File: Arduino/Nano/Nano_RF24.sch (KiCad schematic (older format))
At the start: 3 parts, among them P1 NRF24L01+, U1 Arduino_Nano

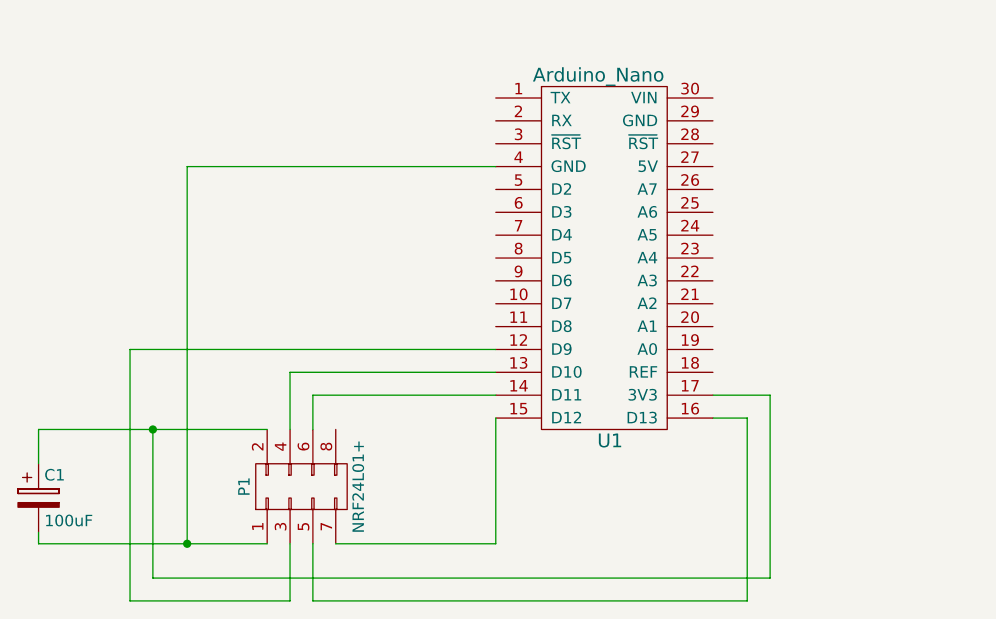
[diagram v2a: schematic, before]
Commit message: v2 with breakout pins
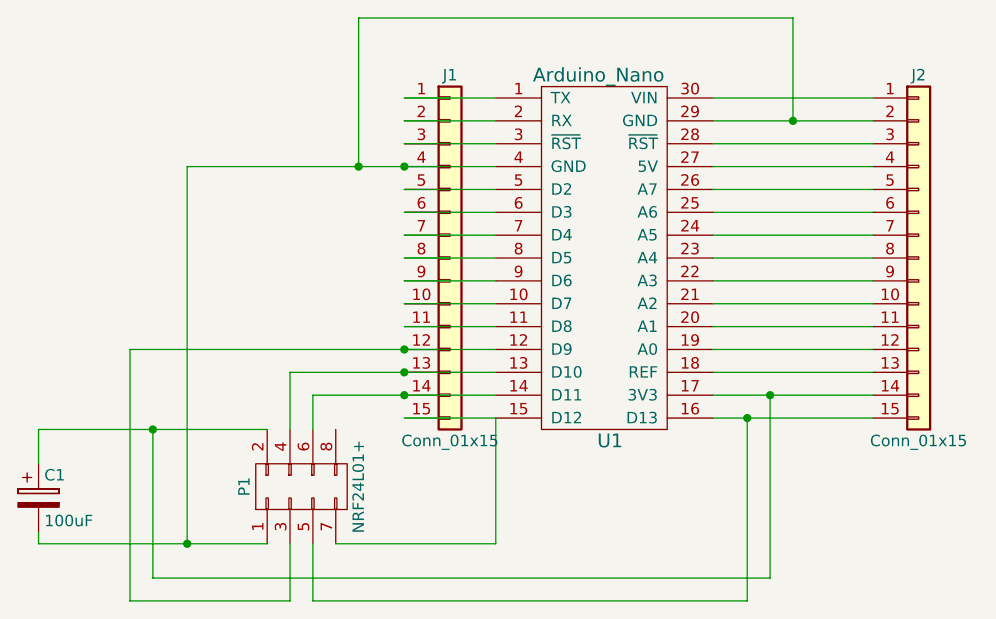
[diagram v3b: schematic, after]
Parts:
- added J1, J2: Conn_01x15, Pin_Headers:Pin_Header_Straight_1x15_Pitch2.54mm, symbol Conn_01x15
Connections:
- net at U1.1 (TX): now also J1.1 (Pin_1)
- net at U1.10 (D7): now also J1.10 (Pin_10)
- net at U1.11 (D8): now also J1.11 (Pin_11)
- net at P1.3 (P3), U1.12 (D9): now also J1.12 (Pin_12)
- net at P1.4 (P4), U1.13 (D10): now also J1.13 (Pin_13)
- net at P1.6 (P6), U1.14 (D11): now also J1.14 (Pin_14)
- net at P1.7 (P7), U1.15 (D12): now also J1.15 (Pin_15)
- net at P1.5 (P5), U1.16 (D13): now also J2.15 (Pin_15)
- net at C1.1, P1.2 (P2), U1.17 (3V3): now also J2.14 (Pin_14)
- net at U1.18 (REF): now also J2.13 (Pin_13)
- net at U1.19 (A0): now also J2.12 (Pin_12)
- net at U1.2 (RX): now also J1.2 (Pin_2)
- net at U1.20 (A1): now also J2.11 (Pin_11)
- net at U1.21 (A2): now also J2.10 (Pin_10)
- net at U1.22 (A3): now also J2.9 (Pin_9)
- net at U1.23 (A4): now also J2.8 (Pin_8)
- net at U1.24 (A5): now also J2.7 (Pin_7)
- net at U1.25 (A6): now also J2.6 (Pin_6)
- net at U1.26 (A7): now also J2.5 (Pin_5)
- net at U1.27 (5V): now also J2.4 (Pin_4)
- net at U1.28 (~RST): now also J2.3 (Pin_3)
- net at U1.29 (GND): now also C1.2, P1.1 (P1), U1.4 (GND), J1.4 (Pin_4), J2.2 (Pin_2)
- net at U1.3 (~RST): now also J1.3 (Pin_3)
- net at U1.30 (VIN): now also J2.1 (Pin_1)
- net at U1.5 (D2): now also J1.5 (Pin_5)
- net at U1.6 (D3): now also J1.6 (Pin_6)
- net at U1.7 (D4): now also J1.7 (Pin_7)
- net at U1.8 (D5): now also J1.8 (Pin_8)
- net at U1.9 (D6): now also J1.9 (Pin_9)
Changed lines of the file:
@@
 Title "Arduino Nano NRF24L01+ Adaptor"
 Date "2018-03-30"
-Rev "1"
+Rev "2"
 Comp ""
 Comment1 "Copyright Mark Benson 2018"
@@
 $EndComp
 Wire Wire Line
-	4900 3150 3550 3150
-Wire Wire Line
 	3550 3150 3550 4800
 Wire Wire Line
@@
 	6100 4950 6100 4150
 Wire Wire Line
-	6100 4150 5850 4150
+	5850 4150 6550 4150
 Wire Wire Line
 	4000 4800 4000 5050
@@
 	3300 5050 3300 3950
 Wire Wire Line
-	3300 3950 4900 3950
-Wire Wire Line
 	4000 4300 4000 4050
-Wire Wire Line
-	4000 4050 4900 4050
 Wire Wire Line
 	4100 4800 4100 5050
@@
 	6000 5050 6000 4250
 Wire Wire Line
-	6000 4250 5850 4250
+	5850 4250 6550 4250
 Wire Wire Line
 	4100 4300 4100 4150
-Wire Wire Line
-	4100 4150 4900 4150
 Wire Wire Line
 	4200 4800 4900 4800
@@
 	2900 4300 2900 4450
 Connection ~ 3400 4300
+$Comp
+L Conn_01x15 J2
+U 1 1 5ABE09D5
+P 6750 3550
+F 0 "J2" H 6750 4350 50  0000 C CNN
+F 1 "Conn_01x15" H 6750 2750 50  0000 C CNN
+F 2 "Pin_Headers:Pin_Header_Straight_1x15_Pitch2.54mm" H 6750 3550 50  0001 C CNN
+F 3 "" H 6750 3550 50  0001 C CNN
+	1    6750 3550
+	1    0    0    -1
+$EndComp
+$Comp
+L Conn_01x15 J1
+U 1 1 5ABE09F4
+P 4700 3550
+F 0 "J1" H 4700 4350 50  0000 C CNN
+F 1 "Conn_01x15" H 4700 2750 50  0000 C CNN
+F 2 "Pin_Headers:Pin_Header_Straight_1x15_Pitch2.54mm" H 4700 3550 50  0001 C CNN
+F 3 "" H 4700 3550 50  0001 C CNN
+	1    4700 3550
+	1    0    0    -1
+$EndComp
+Wire Wire Line
+	5850 2850 6550 2850
+Wire Wire Line
+	5850 2950 6550 2950
+Wire Wire Line
+	5850 3050 6550 3050
+Wire Wire Line
+	5850 3150 6550 3150
+Wire Wire Line
+	5850 3250 6550 3250
+Wire Wire Line
+	5850 3350 6550 3350
+Wire Wire Line
+	5850 3450 6550 3450
+Wire Wire Line
+	5850 3550 6550 3550
+Wire Wire Line
+	6550 3650 5850 3650
+Wire Wire Line
+	5850 3750 6550 3750
+Wire Wire Line
+	5850 3850 6550 3850
+Wire Wire Line
+	5850 3950 6550 3950
+Wire Wire Line
+	5850 4050 6550 4050
+Connection ~ 6100 4150
+Connection ~ 6000 4250
+Wire Wire Line
+	4500 2850 4900 2850
+Wire Wire Line
+	4900 2950 4500 2950
+Wire Wire Line
+	4500 3050 4900 3050
+Wire Wire Line
+	4500 3250 4900 3250
+Wire Wire Line
+	4500 3350 4900 3350
+Wire Wire Line
+	3550 3150 4900 3150
+Connection ~ 4500 3150
+Wire Wire Line
+	4900 3450 4500 3450
+Wire Wire Line
+	4500 3550 4900 3550
+Wire Wire Line
+	4500 3650 4900 3650
+Wire Wire Line
+	4500 3750 4900 3750
+Wire Wire Line
+	4500 3850 4900 3850
+Wire Wire Line
+	3300 3950 4900 3950
+Connection ~ 4500 3950
+Wire Wire Line
+	4000 4050 4900 4050
+Connection ~ 4500 4050
+Wire Wire Line
+	4100 4150 4900 4150
+Connection ~ 4500 4150
+Wire Wire Line
+	4900 4250 4500 4250
+Wire Wire Line
+	4300 3150 4300 2500
+Wire Wire Line
+	4300 2500 6200 2500
+Wire Wire Line
+	6200 2500 6200 2950
+Connection ~ 6200 2950
+Connection ~ 4300 3150
 $EndSCHEMATC
